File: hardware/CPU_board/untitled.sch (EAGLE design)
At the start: 77 parts, among them IC1 MAX232ECWE, IC2 MAX232ECWE, IC3 AM29F040J, IC4 74HCT138D, IC5 LM2596S, IC6 74245SSOP, IC7 74245SSOP, IC8 74245SSOP, J2 POWER_JACKSLT, U1 AS6C4008-55SIN

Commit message: Minor changes in PCB design
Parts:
- added R16, R17, R19, R20, R21: (no value), rcl:R-EU_R0603
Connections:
- net /ACK: now also R21.1
- net /ERR: now also R16.1
- net 5V: now also R16.2, R21.2
- net BUSY: now also R20.2
- net GND: now also R17.1, R19.1, R20.1
- net PE: now also R19.2
- net SLCT: now also R17.2
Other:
- moved on the sheet: R11
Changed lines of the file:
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@@
 <part name="GND74" library="supply1" deviceset="GND" device=""/>
 <part name="C15" library="rcl" deviceset="C-EU" device="C0603"/>
+<part name="R16" library="rcl" deviceset="R-EU_" device="R0603"/>
+<part name="R17" library="rcl" deviceset="R-EU_" device="R0603"/>
+<part name="GND9" library="supply1" deviceset="GND" device=""/>
+<part name="R19" library="rcl" deviceset="R-EU_" device="R0603"/>
+<part name="R20" library="rcl" deviceset="R-EU_" device="R0603"/>
+<part name="R21" library="rcl" deviceset="R-EU_" device="R0603"/>
 </parts>
 <sheets>
@@
 <instance part="IC7" gate="P" x="25.4" y="190.5"/>
 <instance part="IC8" gate="P" x="35.56" y="190.5"/>
-<instance part="R11" gate="G$1" x="345.44" y="226.06" rot="R90"/>
+<instance part="R11" gate="G$1" x="330.2" y="226.06" rot="R90"/>
 <instance part="C24" gate="G$1" x="-58.42" y="190.5"/>
 <instance part="C26" gate="G$1" x="-50.8" y="190.5"/>
@@
 <instance part="GND74" gate="1" x="-48.26" y="104.14"/>
 <instance part="C15" gate="G$1" x="-119.38" y="190.5"/>
+<instance part="R16" gate="G$1" x="347.98" y="241.3" rot="R90"/>
+<instance part="R17" gate="G$1" x="347.98" y="210.82" rot="R90"/>
+<instance part="GND9" gate="1" x="347.98" y="198.12"/>
+<instance part="R19" gate="G$1" x="353.06" y="210.82" rot="R90"/>
+<instance part="R20" gate="G$1" x="358.14" y="210.82" rot="R90"/>
+<instance part="R21" gate="G$1" x="355.6" y="241.3" rot="R90"/>
 </instances>
 <busses>
@@
 <wire x1="-48.26" y1="111.76" x2="-48.26" y2="106.68" width="0.1524" layer="91"/>
 </segment>
+<segment>
+<pinref part="GND9" gate="1" pin="GND"/>
+<pinref part="R17" gate="G$1" pin="1"/>
+<wire x1="347.98" y1="200.66" x2="347.98" y2="203.2" width="0.1524" layer="91"/>
+<pinref part="R19" gate="G$1" pin="1"/>
+<wire x1="347.98" y1="203.2" x2="347.98" y2="205.74" width="0.1524" layer="91"/>
+<wire x1="353.06" y1="205.74" x2="353.06" y2="203.2" width="0.1524" layer="91"/>
+<wire x1="353.06" y1="203.2" x2="347.98" y2="203.2" width="0.1524" layer="91"/>
+<junction x="347.98" y="203.2"/>
+<pinref part="R20" gate="G$1" pin="1"/>
+<wire x1="353.06" y1="203.2" x2="358.14" y2="203.2" width="0.1524" layer="91"/>
+<wire x1="358.14" y1="203.2" x2="358.14" y2="205.74" width="0.1524" layer="91"/>
+<junction x="353.06" y="203.2"/>
+</segment>
 </net>
 <net name="5V" class="0">
@@
 <segment>
 <pinref part="R11" gate="G$1" pin="2"/>
-<wire x1="345.44" y1="231.14" x2="345.44" y2="233.68" width="0.1524" layer="91"/>
-<label x="345.44" y="233.68" size="1.4224" layer="95" rot="R90" xref="yes"/>
+<wire x1="330.2" y1="231.14" x2="330.2" y2="233.68" width="0.1524" layer="91"/>
+<label x="330.2" y="233.68" size="1.4224" layer="95" rot="R90" xref="yes"/>
 </segment>
 <segment>
@@
 <wire x1="-48.26" y1="121.92" x2="-48.26" y2="129.54" width="0.1524" layer="91"/>
 <label x="-48.26" y="129.54" size="1.4224" layer="95" rot="R90" xref="yes"/>
+</segment>
+<segment>
+<pinref part="R16" gate="G$1" pin="2"/>
+<wire x1="347.98" y1="246.38" x2="347.98" y2="248.92" width="0.1524" layer="91"/>
+<pinref part="R21" gate="G$1" pin="2"/>
+<wire x1="347.98" y1="248.92" x2="347.98" y2="251.46" width="0.1524" layer="91"/>
+<wire x1="347.98" y1="248.92" x2="355.6" y2="248.92" width="0.1524" layer="91"/>
+<wire x1="355.6" y1="248.92" x2="355.6" y2="246.38" width="0.1524" layer="91"/>
+<junction x="347.98" y="248.92"/>
 </segment>
 </net>
@@
 <segment>
 <pinref part="IC8" gate="A" pin="A4"/>
-<wire x1="368.3" y1="233.68" x2="360.68" y2="233.68" width="0.1524" layer="91"/>
+<wire x1="368.3" y1="233.68" x2="347.98" y2="233.68" width="0.1524" layer="91"/>
+<label x="345.44" y="233.68" size="1.4224" layer="95" rot="R180" xref="yes"/>
+<pinref part="R16" gate="G$1" pin="1"/>
+<wire x1="347.98" y1="233.68" x2="345.44" y2="233.68" width="0.1524" layer="91"/>
+<wire x1="347.98" y1="236.22" x2="347.98" y2="233.68" width="0.1524" layer="91"/>
+<junction x="347.98" y="233.68"/>
 </segment>
 </net>
@@
 <segment>
 <pinref part="IC8" gate="A" pin="A8"/>
-<wire x1="368.3" y1="223.52" x2="360.68" y2="223.52" width="0.1524" layer="91"/>
-<label x="360.68" y="223.52" size="1.4224" layer="95" rot="R180" xref="yes"/>
+<wire x1="368.3" y1="223.52" x2="355.6" y2="223.52" width="0.1524" layer="91"/>
+<label x="345.44" y="223.52" size="1.4224" layer="95" rot="R180" xref="yes"/>
+<pinref part="R21" gate="G$1" pin="1"/>
+<wire x1="355.6" y1="223.52" x2="345.44" y2="223.52" width="0.1524" layer="91"/>
+<wire x1="355.6" y1="236.22" x2="355.6" y2="223.52" width="0.1524" layer="91"/>
+<junction x="355.6" y="223.52"/>
 </segment>
 </net>
@@
 <segment>
 <pinref part="IC8" gate="A" pin="A7"/>
-<wire x1="368.3" y1="226.06" x2="360.68" y2="226.06" width="0.1524" layer="91"/>
-<label x="360.68" y="226.06" size="1.4224" layer="95" rot="R180" xref="yes"/>
+<wire x1="368.3" y1="226.06" x2="358.14" y2="226.06" width="0.1524" layer="91"/>
+<label x="345.44" y="226.06" size="1.4224" layer="95" rot="R180" xref="yes"/>
+<pinref part="R20" gate="G$1" pin="2"/>
+<wire x1="358.14" y1="226.06" x2="345.44" y2="226.06" width="0.1524" layer="91"/>
+<wire x1="358.14" y1="215.9" x2="358.14" y2="226.06" width="0.1524" layer="91"/>
+<junction x="358.14" y="226.06"/>
 </segment>
 </net>
@@
 <segment>
 <pinref part="IC8" gate="A" pin="A6"/>
-<wire x1="368.3" y1="228.6" x2="360.68" y2="228.6" width="0.1524" layer="91"/>
-<label x="360.68" y="228.6" size="1.4224" layer="95" rot="R180" xref="yes"/>
+<wire x1="368.3" y1="228.6" x2="353.06" y2="228.6" width="0.1524" layer="91"/>
+<label x="345.44" y="228.6" size="1.4224" layer="95" rot="R180" xref="yes"/>
+<pinref part="R19" gate="G$1" pin="2"/>
+<wire x1="353.06" y1="228.6" x2="345.44" y2="228.6" width="0.1524" layer="91"/>
+<wire x1="353.06" y1="215.9" x2="353.06" y2="228.6" width="0.1524" layer="91"/>
+<junction x="353.06" y="228.6"/>
 </segment>
 </net>
@@
 <segment>
 <pinref part="IC8" gate="A" pin="A5"/>
-<wire x1="368.3" y1="231.14" x2="360.68" y2="231.14" width="0.1524" layer="91"/>
-<label x="360.68" y="231.14" size="1.4224" layer="95" rot="R180" xref="yes"/>
+<wire x1="368.3" y1="231.14" x2="347.98" y2="231.14" width="0.1524" layer="91"/>
+<label x="345.44" y="231.14" size="1.4224" layer="95" rot="R180" xref="yes"/>
+<pinref part="R17" gate="G$1" pin="2"/>
+<wire x1="347.98" y1="231.14" x2="345.44" y2="231.14" width="0.1524" layer="91"/>
+<wire x1="347.98" y1="215.9" x2="347.98" y2="231.14" width="0.1524" layer="91"/>
+<junction x="347.98" y="231.14"/>
 </segment>
 </net>
@@
 <pinref part="IC8" gate="A" pin="DIR"/>
 <pinref part="R11" gate="G$1" pin="1"/>
-<wire x1="368.3" y1="218.44" x2="345.44" y2="218.44" width="0.1524" layer="91"/>
-<wire x1="345.44" y1="218.44" x2="345.44" y2="220.98" width="0.1524" layer="91"/>
-</segment>
-</net>
+<wire x1="368.3" y1="218.44" x2="330.2" y2="218.44" width="0.1524" layer="91"/>
+<wire x1="330.2" y1="218.44" x2="330.2" y2="220.98" width="0.1524" layer="91"/>
+</segment>
+</net>

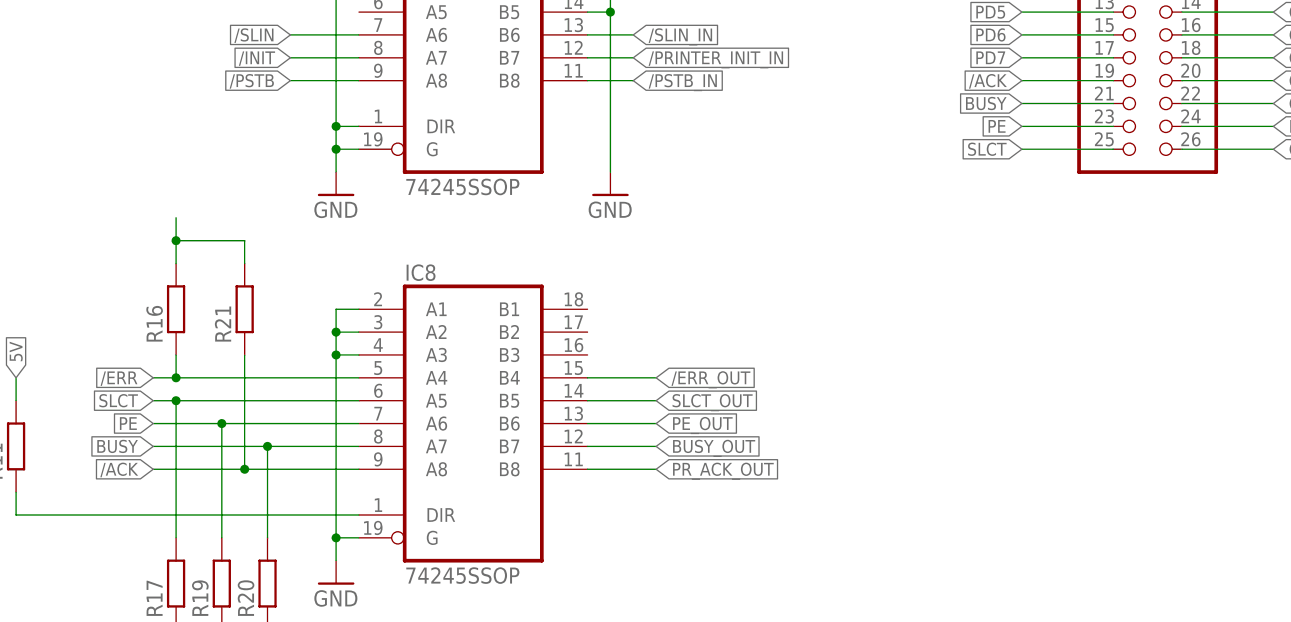
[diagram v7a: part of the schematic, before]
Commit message: PCB updated - resistors protecting default output lines at reset
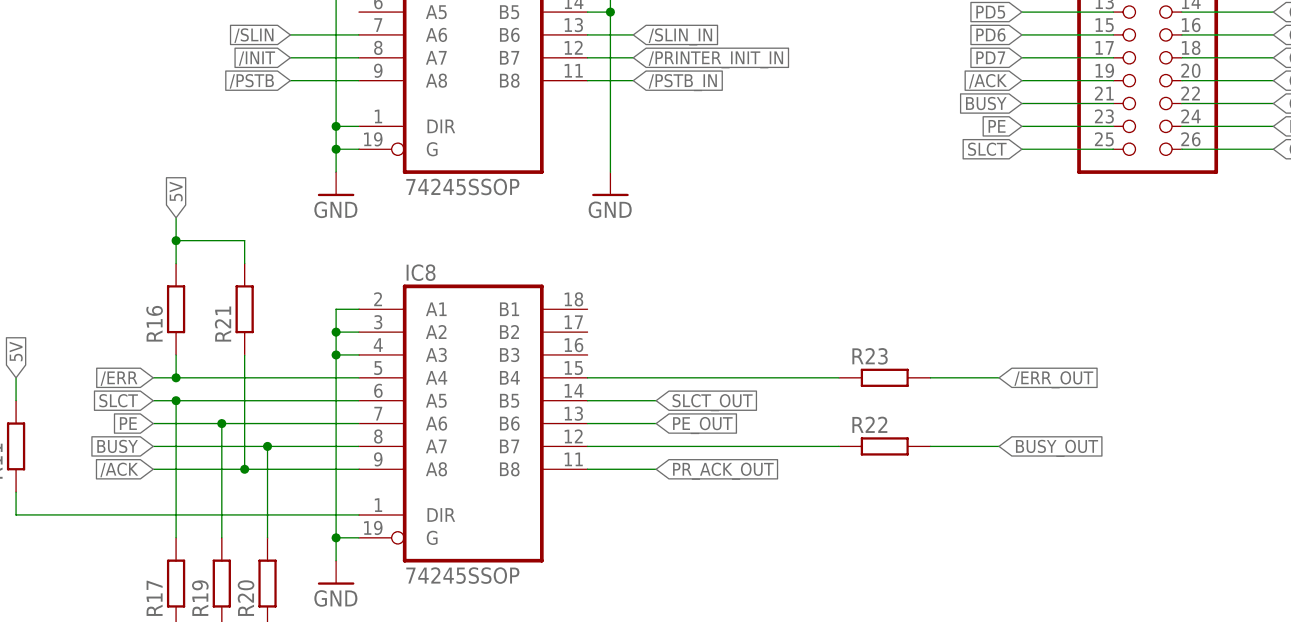
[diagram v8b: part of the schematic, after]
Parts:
- added R22, R23: (no value), rcl:R-EU_R0402
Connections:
- new net N$46: IC8A.B7, R22.1
- new net N$47: IC8A.B4, R23.1
- net /ERR_OUT: now also R23.2; no longer IC8A.B4
- net BUSY_OUT: now also R22.2; no longer IC8A.B7
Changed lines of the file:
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@@
 <part name="R20" library="rcl" deviceset="R-EU_" device="R0603"/>
 <part name="R21" library="rcl" deviceset="R-EU_" device="R0603"/>
+<part name="R22" library="rcl" deviceset="R-EU_" device="R0402"/>
+<part name="R23" library="rcl" deviceset="R-EU_" device="R0402"/>
 </parts>
 <sheets>
@@
 <instance part="R20" gate="G$1" x="358.14" y="210.82" rot="R90"/>
 <instance part="R21" gate="G$1" x="355.6" y="241.3" rot="R90"/>
+<instance part="R22" gate="G$1" x="426.72" y="226.06"/>
+<instance part="R23" gate="G$1" x="426.72" y="233.68"/>
 </instances>
 <busses>
@@
 <wire x1="355.6" y1="248.92" x2="355.6" y2="246.38" width="0.1524" layer="91"/>
 <junction x="347.98" y="248.92"/>
+<label x="347.98" y="251.46" size="1.4224" layer="95" rot="R90" xref="yes"/>
 </segment>
 </net>
@@
 <net name="BUSY_OUT" class="0">
 <segment>
-<pinref part="IC8" gate="A" pin="B7"/>
-<wire x1="393.7" y1="226.06" x2="401.32" y2="226.06" width="0.1524" layer="91"/>
-<label x="401.32" y="226.06" size="1.4224" layer="95" xref="yes"/>
+<label x="439.42" y="226.06" size="1.4224" layer="95" xref="yes"/>
+<pinref part="R22" gate="G$1" pin="2"/>
+<wire x1="431.8" y1="226.06" x2="439.42" y2="226.06" width="0.1524" layer="91"/>
 </segment>
 <segment>
@@
 <net name="/ERR_OUT" class="0">
 <segment>
-<wire x1="393.7" y1="233.68" x2="401.32" y2="233.68" width="0.1524" layer="91"/>
-<pinref part="IC8" gate="A" pin="B4"/>
-<label x="401.32" y="233.68" size="1.4224" layer="95" xref="yes"/>
+<label x="439.42" y="233.68" size="1.4224" layer="95" xref="yes"/>
+<pinref part="R23" gate="G$1" pin="2"/>
+<wire x1="431.8" y1="233.68" x2="439.42" y2="233.68" width="0.1524" layer="91"/>
 </segment>
 <segment>
@@
 </segment>
 </net>
+<net name="N$46" class="0">
+<segment>
+<pinref part="R22" gate="G$1" pin="1"/>
+<pinref part="IC8" gate="A" pin="B7"/>
+<wire x1="393.7" y1="226.06" x2="421.64" y2="226.06" width="0.1524" layer="91"/>
+</segment>
+</net>
+<net name="N$47" class="0">
+<segment>
+<pinref part="R23" gate="G$1" pin="1"/>
+<pinref part="IC8" gate="A" pin="B4"/>
+<wire x1="393.7" y1="233.68" x2="421.64" y2="233.68" width="0.1524" layer="91"/>
+</segment>
+</net>
